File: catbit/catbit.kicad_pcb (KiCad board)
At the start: 2 copper layers, 52 x 29.5 mm, 11 parts, among them J1 5V LED Laser, J2 ServoX, J3 ServoY, J4 5V DC in, Q1 2N7000, U1 LD33

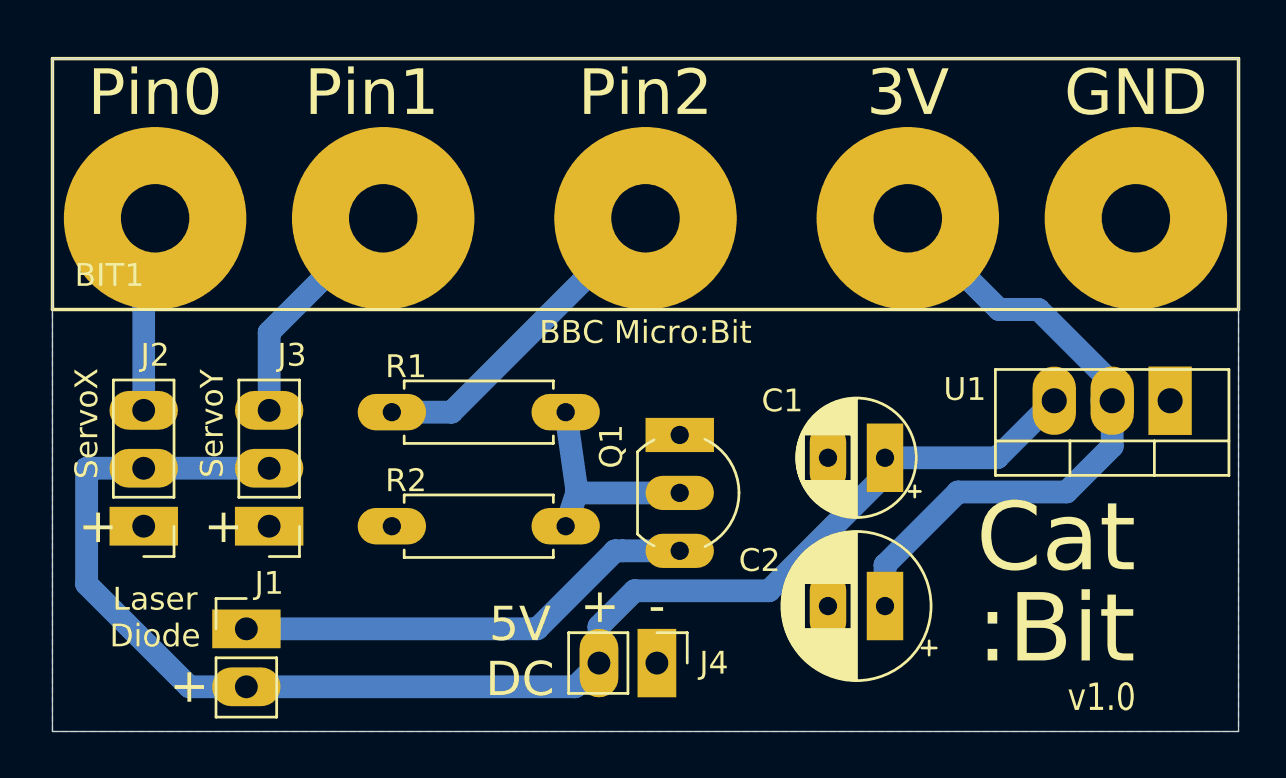
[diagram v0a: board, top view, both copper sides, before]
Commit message: Revised (V2) PCB with led.
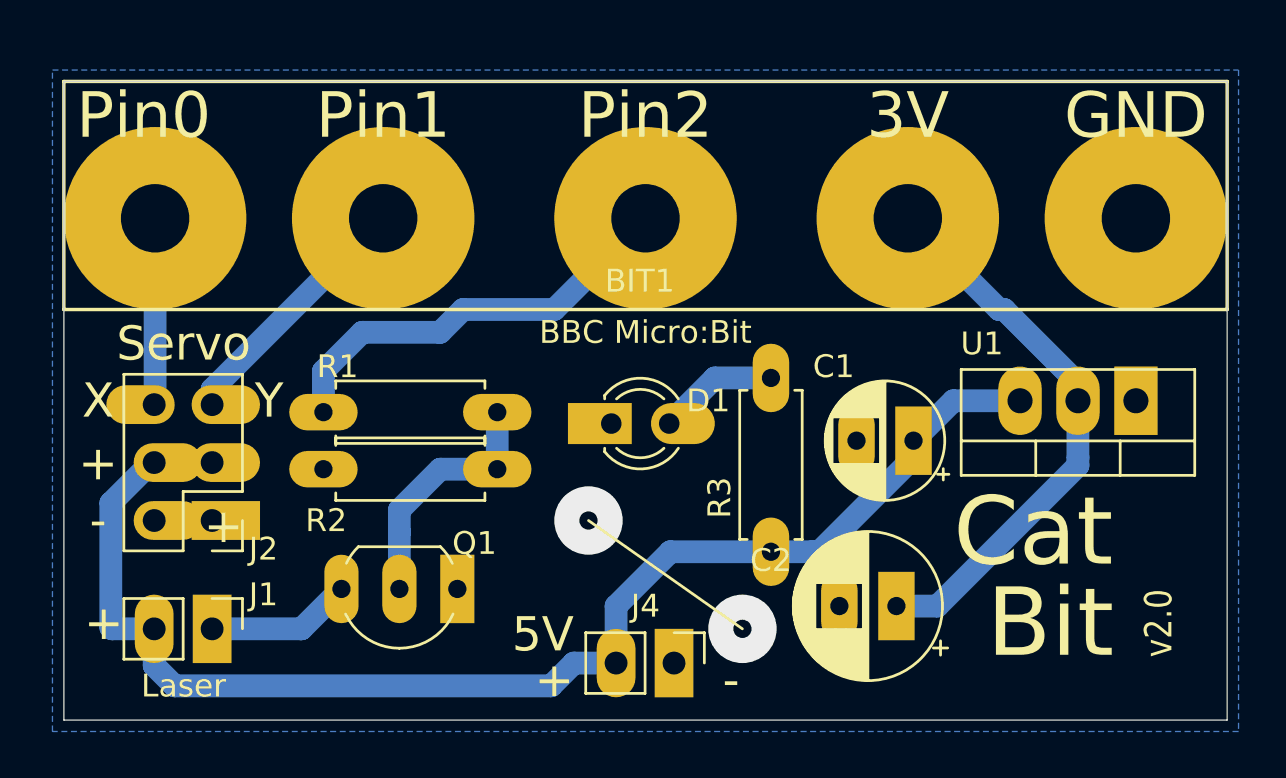
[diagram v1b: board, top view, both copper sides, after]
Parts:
- removed J3: ServoY, Connector_PinHeader_2.54mm:PinHeader_1x03_P2.54mm_Vertical
- added D1: Pwr, LED_THT:LED_D3.0mm, F.Cu at (150.8, 138.9)
- added R3: 330R, Resistor_THT:R_Axial_DIN0207_L6.3mm_D2.5mm_P7.62mm_Horizontal, F.Cu at (157.8, 136.9)
- BIT1: footprint catbit:MicroBit -> microbit:MicroBit
- J2: value ServoX -> Servos; footprint Connector_PinHeader_2.54mm:PinHeader_1x03_P2.54mm_Vertical -> Connector_PinHeader_2.54mm:PinHeader_2x03_P2.54mm_Vertical
- moved Q1 11.9 mm to (144.1, 146.2), turned to 180 degrees
- moved R2 3.91 mm to (138.2, 140.9)
- moved J2 3.01 mm to (133.3, 143.2)
- moved R1 3.00 mm to (145.8, 138.4)
- moved J1 1.50 mm to (133.3, 147.9), turned to 270 degrees
- moved U1 1.50 mm to (173.8, 137.9)
- moved C1 1.46 mm to (164.1, 139.7)
- moved J4 0.75 mm to (153.6, 149.4)
- moved C2 0.50 mm to (163.3, 146.9)
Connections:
- J2 pad 2: 5V -> GND
- J2 pad 3: X -> 5V
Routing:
- net Net-(J1-Pad1): track 20.4 -> 6.39 mm
- net Net-(D1-Pad2): track 0.00 -> 5.29 mm
- net 5V: track 64.1 -> 59.6 mm
- net 3V: track 29.1 -> 24.6 mm
- net LASER: track 14.6 -> 18.7 mm
- net GND: track 0.00 -> 2.54 mm, vias 0 -> 2
- net Net-(Q1-Pad2): track 9.58 -> 11.0 mm
- net Y: track 10.5 -> 11.3 mm
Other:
- board size 52 x 29.5 mm -> 51 x 28 mm
- net class Default: via_dia 0.8 -> 3; via_drill 0.4 -> 0.8
- board text added: "5V"
- board text added: "Bit"
- board text added: "Laser"
- board text added: "Servo"
- board text added: "X"
- board text added: "Y"
- board text added: "v2.0"
- board text removed: "5V DC"
- board text removed: ":Bit"
- board text removed: "Laser Diode"
- board text removed: "ServoX"
- board text removed: "ServoY"
- board text removed: "v1.0"

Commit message: Minor silkscreen mod and move aux. axis to bottom-left corner (easier to set up cnc)
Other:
- board text added: "link"
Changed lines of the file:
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@@
   (general
     (thickness 1.6)
-    (drawings 20)
+    (drawings 21)
     (tracks 50)
     (zones 0)
@@
     (pad_to_mask_clearance 0.051)
     (solder_mask_min_width 0.25)
-    (aux_axis_origin 152.3 129.9)
+    (aux_axis_origin 126.8 151.9)
     (grid_origin 152.3 129.9)
     (visible_elements FFFFFF7F)
@@
     (descr "Through hole straight pin header, 1x02, 2.54mm pitch, single row")
     (tags "Through hole pin header THT 1x02 2.54mm single row")
-    (fp_text reference J4 (at -2.5 1.25 180) (layer F.SilkS)
+    (fp_text reference J4 (at -0.75 -2.25 180) (layer F.SilkS)
       (effects (font (size 1 1) (thickness 0.15)))
     )
@@
     )
   )
+  (gr_text link (at 153.05 144.65 -35) (layer F.SilkS)
+    (effects (font (size 1 1) (thickness 0.15)))
+  )
   (gr_line (start 156.55 147.9) (end 149.8 143.15) (layer F.SilkS) (width 0.12))
